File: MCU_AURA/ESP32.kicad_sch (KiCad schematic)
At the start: 15 parts, among them J200 TC2050-IDC-430, U200 ESP32-S3-WROOM-1, U201 USBLC6-2SC6

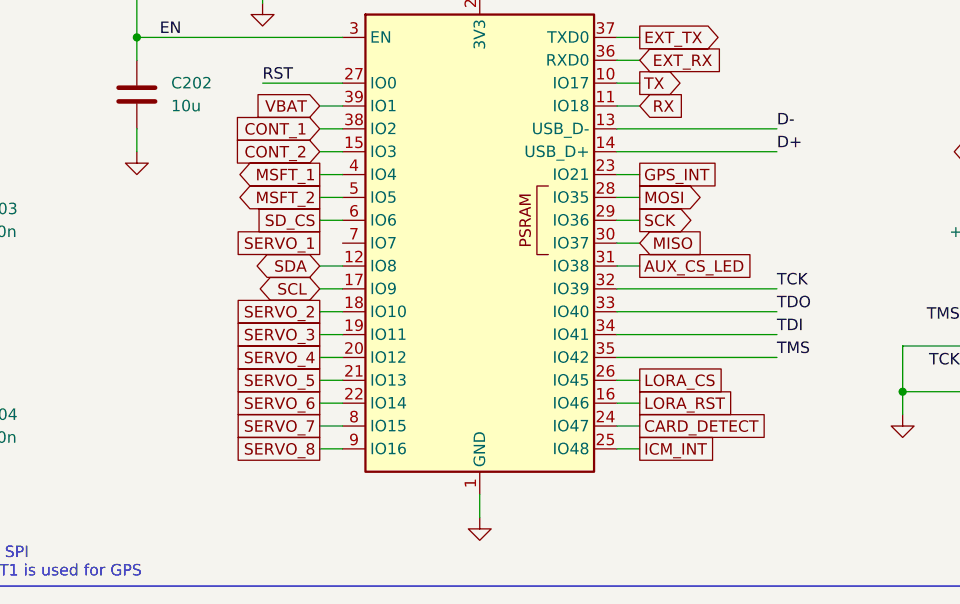
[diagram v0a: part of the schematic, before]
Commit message: Started Editing
Problem syncing desktop to laptop (libraries).
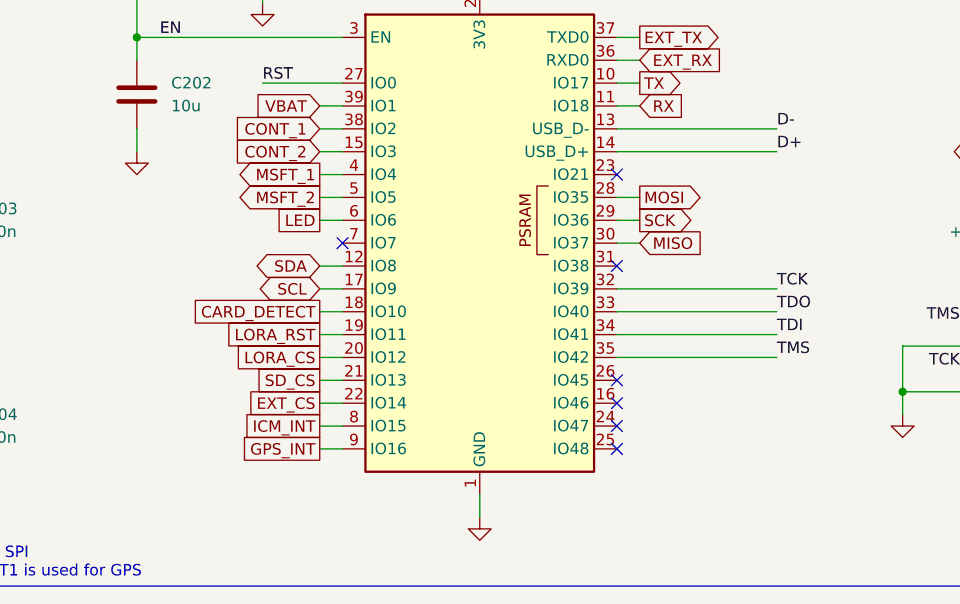
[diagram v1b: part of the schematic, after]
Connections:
- net SERVO_2 is gone; now on net CARD_DETECT: U200.18 (IO10)
- net SERVO_3 is gone; now on net LORA_RST: U200.19 (IO11)
- net SERVO_4 is gone; now on net LORA_CS: U200.20 (IO12)
- net SERVO_5 is gone; now on net SD_CS: U200.21 (IO13)
- net SERVO_7 is gone; now on net ICM_INT: U200.8 (IO15)
- net SERVO_8 is gone; now on net GPS_INT: U200.9 (IO16)
- net CARD_DETECT: no longer U200.24 (IO47)
- net GPS_INT: no longer U200.23 (IO21)
- net ICM_INT: no longer U200.25 (IO48)
- net LORA_CS: no longer U200.26 (IO45)
- net LORA_RST: no longer U200.16 (IO46)
- net SD_CS: no longer U200.6 (IO6)
- net AUX_CS_LED: no longer names the net of U200.31 (IO38)
- net SERVO_6 renamed EXT_CS
- new net LED: U200.6 (IO6)
- no-connect marks 5 -> 12

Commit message: Added Samacsys libraries
Made the libraries from the component search engine local.
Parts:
- S200, S201: footprint SamacSys_Parts:EVQPUC02K -> EVQ-PUC02k:EVQPUC02K
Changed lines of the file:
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@@
 			)
 		)
-		(property "Footprint" "SamacSys_Parts:EVQPUC02K"
+		(property "Footprint" "EVQ-PUC02k:EVQPUC02K"
 			(at 66.04 21.92 0)
 			(effects
@@
 			)
 		)
-		(property "Footprint" "SamacSys_Parts:EVQPUC02K"
+		(property "Footprint" "EVQ-PUC02k:EVQPUC02K"
 			(at 66.04 -0.94 0)
 			(effects

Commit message: Synchronised
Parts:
- removed J200: TC2050-IDC-430, TC2050-IDC, symbol SamacSys_Parts:TC2050-IDC-430
- removed S200, S201: EVQ-PUC02K, EVQ-PUC02k:EVQPUC02K, symbol SamacSys_Parts:EVQ-PUC02K
- added J2: TC2050-IDC-430, TC2050-IDC:TC2050-IDC, symbol TC2050-IDC:TC2050-IDC-430
- added S1, S2: EVQ-PUC02K, EVQ-PUC02k:EVQPUC02K, symbol EVQ-PUC02K:EVQ-PUC02K
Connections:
- net +3V3: now also J2.1
- net EN: now also S2.2 (COM_1)
- net GND: now also J2.3, J2.5, J2.7, J2.9, S1.3 (NO_2), S2.3 (NO_2)
- net RST: now also S1.2 (COM_1)
- net TCK: now also J2.4
- net TDI: now also J2.8
- net TDO: now also J2.6
- net TMS: now also J2.2

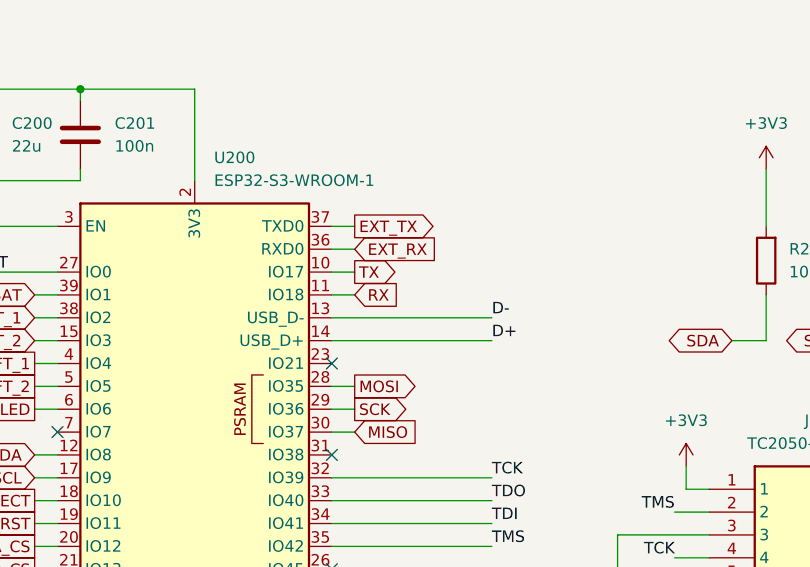
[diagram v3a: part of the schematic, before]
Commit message: Adding 3D Models
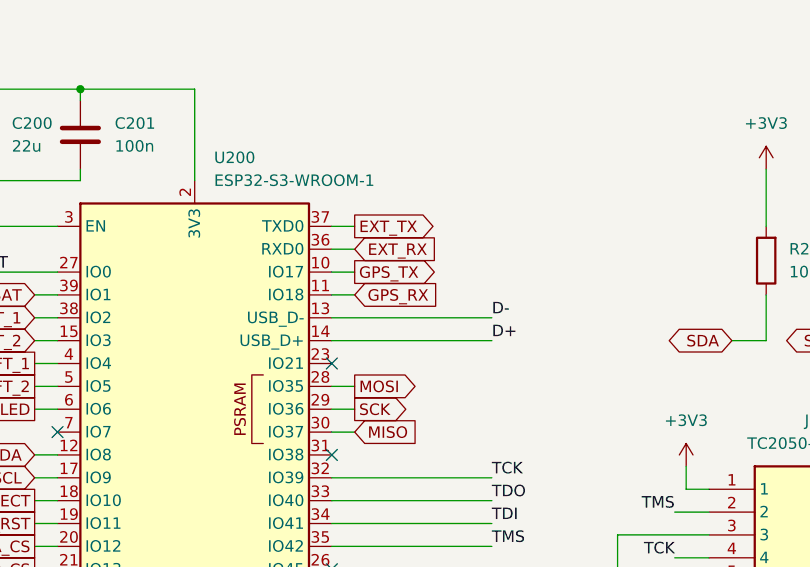
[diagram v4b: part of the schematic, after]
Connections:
- net RX renamed GPS_RX
- net TX renamed GPS_TX
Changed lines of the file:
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@@
 		)
 	)
-	(global_label "TX"
+	(global_label "GPS_TX"
 		(shape output)
 		(at 171.45 83.82 0)
@@
 		)
 		(property "Intersheetrefs" "${INTERSHEET_REFS}"
-			(at 176.6123 83.82 0)
+			(at 181.3294 83.82 0)
 			(effects
 				(font
@@
 		)
 	)
-	(global_label "RX"
+	(global_label "GPS_RX"
 		(shape input)
 		(at 171.45 86.36 0)
@@
 		)
 		(property "Intersheetrefs" "${INTERSHEET_REFS}"
-			(at 176.9147 86.36 0)
+			(at 181.6318 86.36 0)
 			(effects
 				(font

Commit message: Adding Connectors
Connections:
- net EXT_CS: now also U200.7 (IO7); no longer U200.22 (IO14)
- net LED: now also U200.22 (IO14); no longer U200.6 (IO6)
- net LORA_CS renamed RF_CS
- net LORA_RST renamed RF_RST
- new net EXT_RST: U200.6 (IO6)
- no-connect marks 12 -> 11

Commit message: Initial Schematic Draft
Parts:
- renumbered J2 to J200, S1 to S200, S2 to S201
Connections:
- net CONT_1: no longer names the net of U200.38 (IO2)
- net CONT_2: no longer names the net of U200.15 (IO3)
- net VBAT: no longer names the net of U200.39 (IO1)
- no-connect marks 11 -> 14
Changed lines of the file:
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@@
 	)
 	(no_connect
+		(at 138.43 86.36)
+	)
+	(no_connect
+		(at 138.43 88.9)
+	)
+	(no_connect
 		(at 168.91 119.38)
 	)
@@
 	)
 	(no_connect
+		(at 138.43 91.44)
+	)
+	(no_connect
 		(at 168.91 104.14)
 	)
@@
 	(wire
 		(pts
-			(xy 135.89 91.44) (xy 138.43 91.44)
-		)
-		(stroke
-			(width 0)
-			(type default)
-		)
-	)
-	(wire
-		(pts
 			(xy 243.84 120.65) (xy 243.84 115.57)
 		)
@@
 	(wire
 		(pts
-			(xy 135.89 86.36) (xy 138.43 86.36)
-		)
-		(stroke
-			(width 0)
-			(type default)
-		)
-	)
-	(wire
-		(pts
-			(xy 135.89 88.9) (xy 138.43 88.9)
-		)
-		(stroke
-			(width 0)
-			(type default)
-		)
-	)
-	(wire
-		(pts
 			(xy 200.66 118.11) (xy 200.66 120.65)
 		)
@@
 		)
 	)
-	(global_label "CONT_1"
-		(shape input)
-		(at 135.89 88.9 180)
-		(fields_autoplaced yes)
-		(effects
-			(font
-				(size 1.27 1.27)
-			)
-			(justify right)
-		)
-		(property "Intersheetrefs" "${INTERSHEET_REFS}"
-			(at 125.8291 88.9 0)
-			(effects
-				(font
-					(size 1.27 1.27)
-				)
-				(justify right)
-				(hide yes)
-			)
-		)
-	)
 	(global_label "EXT_TX"
 		(shape output)
@@
 		)
 	)
-	(global_label "VBAT"
-		(shape input)
-		(at 135.89 86.36 180)
-		(fields_autoplaced yes)
-		(effects
-			(font
-				(size 1.27 1.27)
-			)
-			(justify right)
-		)
-		(property "Intersheetrefs" "${INTERSHEET_REFS}"
-			(at 128.49 86.36 0)
-			(effects
-				(font
-					(size 1.27 1.27)
-				)
-				(justify right)
-				(hide yes)
-			)
-		)
-	)
-	(global_label "CONT_2"
-		(shape input)
-		(at 135.89 91.44 180)
-		(fields_autoplaced yes)
-		(effects
-			(font
-				(size 1.27 1.27)
-			)
-			(justify right)
-		)
-		(property "Intersheetrefs" "${INTERSHEET_REFS}"
-			(at 125.8291 91.44 0)
-			(effects
-				(font
-					(size 1.27 1.27)
-				)
-				(justify right)
-				(hide yes)
-			)
-		)
-	)
 	(global_label "EXT_CS"
 		(shape passive)
@@
 		(dnp no)
 		(fields_autoplaced yes)
-		(property "Reference" "J2"
+		(property "Reference" "J200"
 			(at 222.25 100.33 0)
 			(effects
@@
 			(project ""
 				(path "/c0b09de1-c640-438f-9ef5-dda14a6aac71/b7286ff6-080d-4fe9-98ea-7dd25e1f4a61"
-					(reference "J2")
+					(reference "J200")
 					(unit 1)
 				)
@@
 		(dnp no)
 		(fields_autoplaced yes)
-		(property "Reference" "S1"
+		(property "Reference" "S200"
 			(at 77.47 83.82 0)
 			(effects
@@
 			(project ""
 				(path "/c0b09de1-c640-438f-9ef5-dda14a6aac71/b7286ff6-080d-4fe9-98ea-7dd25e1f4a61"
-					(reference "S1")
+					(reference "S200")
 					(unit 1)
 				)
@@
 		(dnp no)
 		(fields_autoplaced yes)
-		(property "Reference" "S2"
+		(property "Reference" "S201"
 			(at 77.47 106.68 0)
 			(effects
@@
 			(project "MCU_AURA"
 				(path "/c0b09de1-c640-438f-9ef5-dda14a6aac71/b7286ff6-080d-4fe9-98ea-7dd25e1f4a61"
-					(reference "S2")
+					(reference "S201")
 					(unit 1)
 				)

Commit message: Started Routing
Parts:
- added JP200: SolderJumper_2_Bridged, Jumper:SolderJumper-2_P1.3mm_Open_RoundedPad1.0x1.5mm, symbol Jumper:SolderJumper_2_Bridged
- added R1, R2: 22R, Resistor_SMD:R_0402_1005Metric, symbol Device:R
- J200: now left out of the parts list
- R201, R202: value 27R -> 22R
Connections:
- net +3V3: now also JP200.1 (A); no longer J200.1
- net EN: now also C203.1, S200.3 (NO_2); no longer C204.1, S201.2 (COM_1)
- net GND: now also S200.2 (COM_1), S201.2 (COM_1); no longer S200.3 (NO_2), S201.3 (NO_2)
- net ICM_INT: now also U200.38 (IO2); no longer U200.8 (IO15)
- net RST: now also C204.1, S201.3 (NO_2); no longer C203.1, S200.2 (COM_1)
- net TCK: now also R1.2; no longer U200.32 (IO39)
- net TDO: now also R2.2; no longer U200.33 (IO40)
- net RC_RX: now reaches U200.39 (IO1)
- new net JTAG_3V3: J200.1, JP200.2 (B)
- new net TCK_D: R1.1, U200.32 (IO39)
- new net TDO_D: R2.1, U200.33 (IO40)
- no-connect marks 14 -> 13
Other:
- moved on the sheet: C203, C204, J200

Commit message: First fully routed version
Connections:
- net ICM_INT: now also U200.31 (IO38); no longer U200.38 (IO2)
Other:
- moved on the sheet: C200, C201, C202, J200, JP200, R1, R2, R200, R205, R206, U200
